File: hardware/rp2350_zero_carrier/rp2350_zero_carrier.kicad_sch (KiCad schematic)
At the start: 10 parts, among them J1 RP2350-Zero_Header(23pin,GPIO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, J2 USB-A_Host(Neltron_5075AR-04-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, J3 RP2350-Zero_Header(23pin,ボード2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, SW1 1回路2接点スイッチ(3pin,NKK_115643,ON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, SW2 1回路2接点スイッチ(3pin,NKK_115643,ON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, SW3 1回路2接点スイッチ(3pin,NKK_115643,ON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, SW4 1回路2接点スイッチ(3pin,NKK_115643,ON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

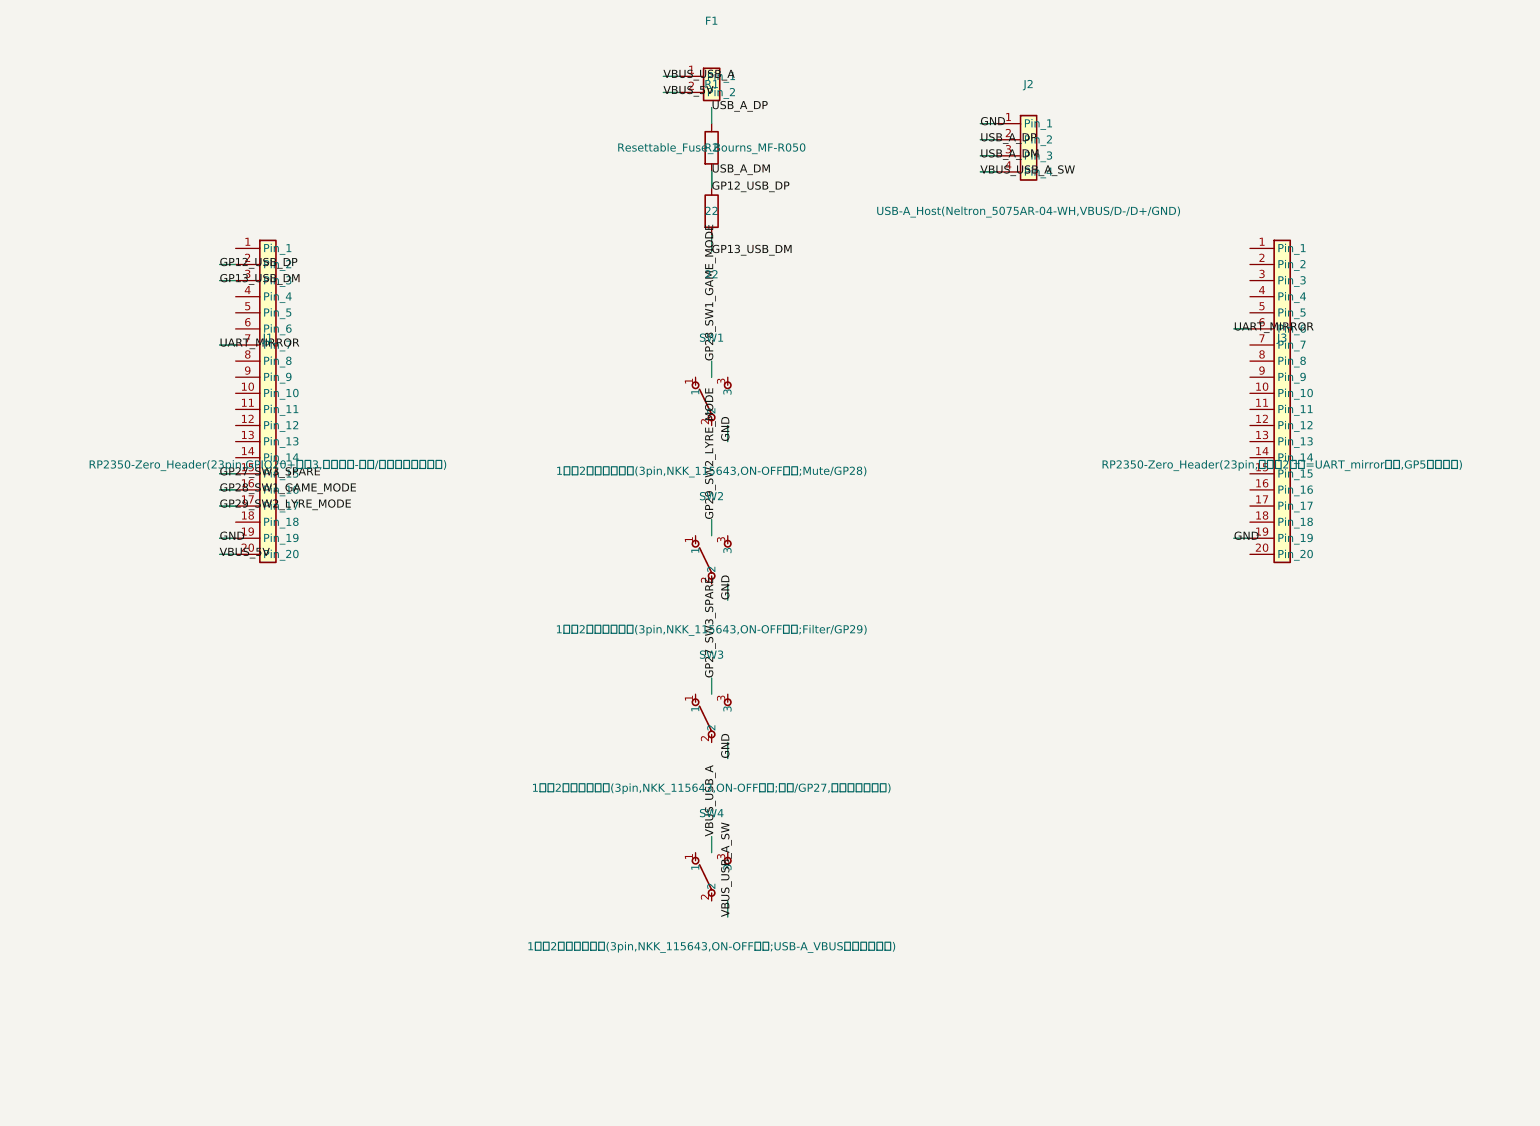
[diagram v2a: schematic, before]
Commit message: SW5(サステインスイッチ)・SW6(MIDI RESETタクトスイッチ)を回路図に追加、UART0デバッグ用ネットも定義
- SW5: SW1-4と同一のSW_SPDT_NKK_115643_Slideを再利用。中央コモンをJ3のGP29
  (net GP29_SW5_SUSTAIN)へ、片側接点をGNDへ、残り1接点はNC(issue #8のサステイン
  スイッチ、ファームはPR #9で対応済み)。
- SW6: 汎用Connector_Generic:Conn_01x04を4pinタクトスイッチの回路図表現として
  流用(内部結線が未確定なため、pin1/2をGND、pin3/4をJ3のGP28(net
  GP28_SW6_RESET)へそれぞれ束ねる防御的配線。issue #6のMIDI RESETボタン、
  ファームはPR #9で対応済み)。
- UART0デバッグ(GP0=TX/GP1=RX)をJ1・J3それぞれの回路図ピンからラベル引き出しの
  みで露出(GP0_UART0_TX/GP1_UART0_RX = J1側、J3_GP0_UART0_TX/J3_GP1_UART0_RX =
  J3側)。ユーザー指示によりピンヘッダ部品は置かず、基板側のみでテストポイントの
  スルーホールを用意する(pcb側の対応footprintは別コミット)。

kicad-cli sch erc で確認: 新規追加分はすべて既存パターンと同種の警告
(endpoint_off_grid / isolated_pin_label 等、手書きスキーマ全体に元々ある
傾向)にとどまり、新しい種類の問題は無い。pin_not_connectedはむしろ
42→39件に減少(J1/J3のGP0/GP1ピンが新規接続されたため)。

Co-Authored-By: Claude Sonnet 5 <noreply@anthropic.com>
Claude-Session: https://claude.ai/code/session_01AwWZfQU4trNEZXtx5MYHvu
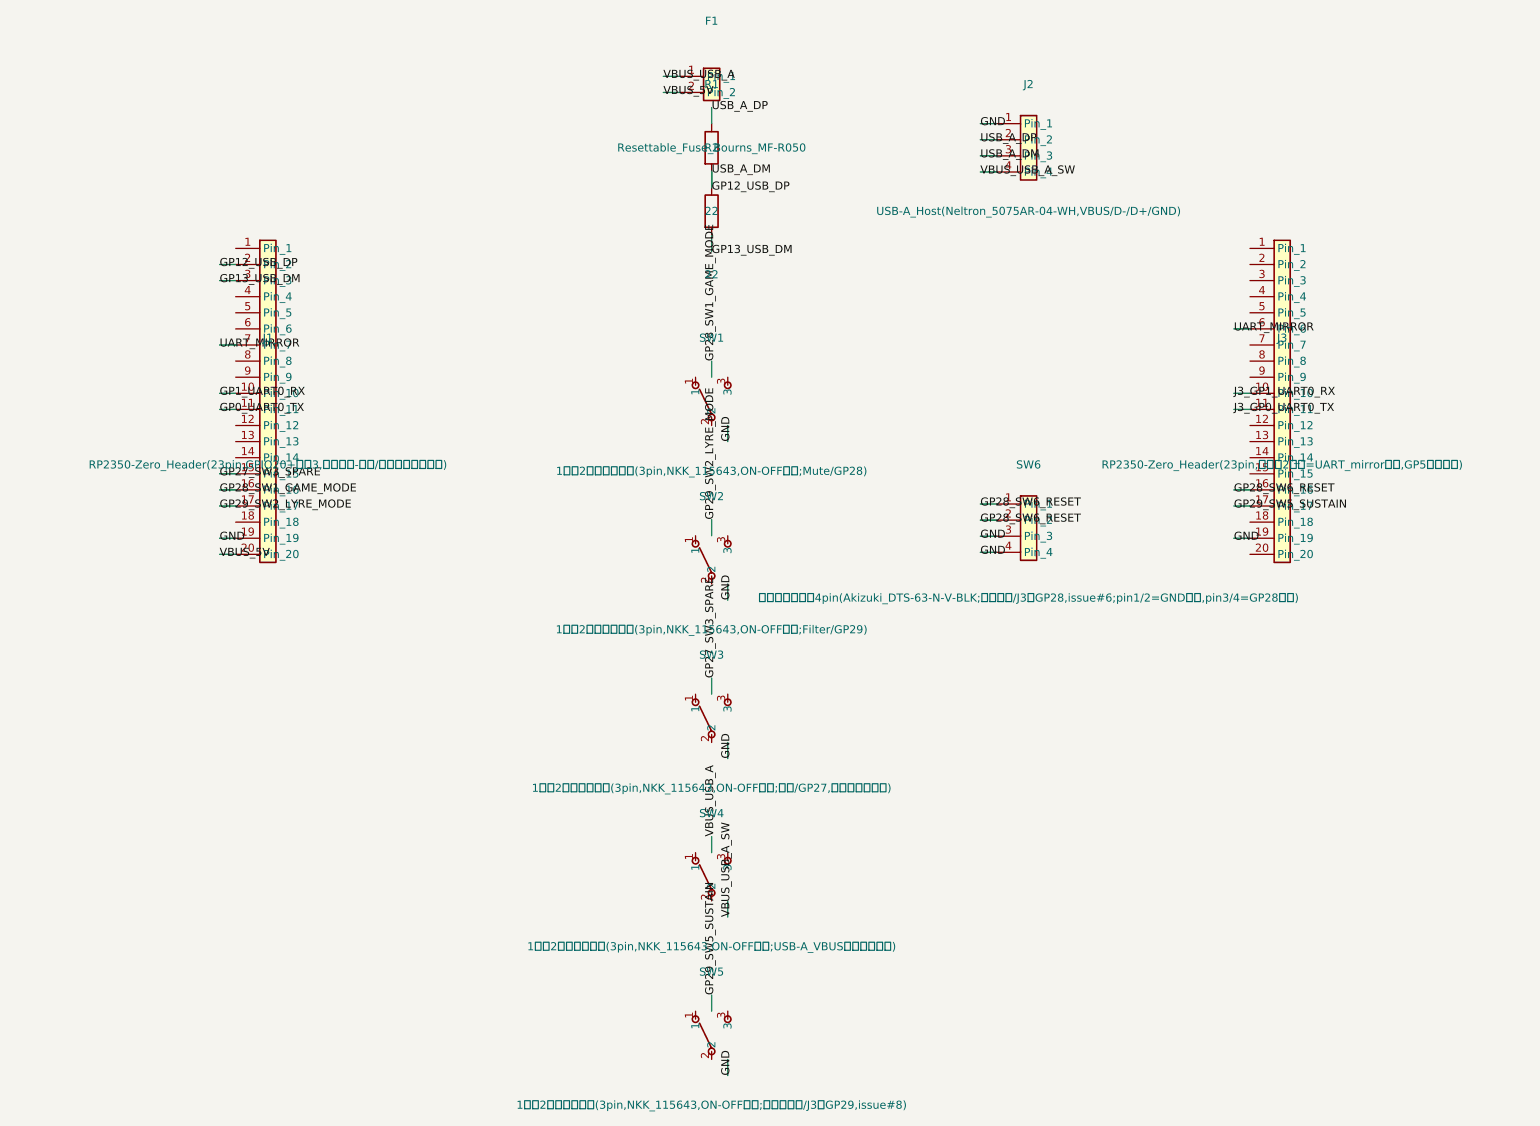
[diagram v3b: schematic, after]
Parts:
- added SW5: 1回路2接点スイッチ(3pin,NKK_115643,ON-OFF用途;サステイン/J3のGP29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, rp2350_zero_carrier:SW_SPDT_NKK_115643_Slide, symbol Switch:SW_SPDT
- added SW6: タクトスイッチ4pin(Akizuki_DTS-63-N-V-BLK;リセット/J3のGP28,i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, rp2350_zero_carrier:SW_TACT_Akizuki_DTS63, symbol Connector_Generic:Conn_01x04
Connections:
- net GND: now also SW6.3 (Pin_3), SW6.4 (Pin_4)
- net GP1_UART0_RX: now reaches J1.10 (Pin_10)
- net GP0_UART0_TX: now reaches J1.11 (Pin_11)
- net J3_GP1_UART0_RX: now reaches J3.10 (Pin_10)
- net J3_GP0_UART0_TX: now reaches J3.11 (Pin_11)
- net GP28_SW6_RESET: now reaches J3.16 (Pin_16)
- net GP28_SW6_RESET: now also SW6.1 (Pin_1), SW6.2 (Pin_2)
- net GP29_SW5_SUSTAIN: now reaches J3.17 (Pin_17)
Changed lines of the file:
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@@
+    )
+  )
+  (symbol (lib_id "Switch:SW_SPDT") (at 110 230 0) (unit 1)
+    (in_bom yes) (on_board yes) (dnp no) (fields_autoplaced yes)
+    (property "Reference" "SW5" (at 110 220 0) (effects (font (size 1.27 1.27))))
+    (property "Value" "1回路2接点スイッチ(3pin,NKK_115643,ON-OFF用途;サステイン/J3のGP29,issue#8)" (at 110 241 0) (effects (font (size 1.27 1.27))))
+    (property "Footprint" "rp2350_zero_carrier:SW_SPDT_NKK_115643_Slide" (at 110 230 0) (effects (font (size 1.27 1.27)) hide))
+    (property "Datasheet" "" (at 110 230 0) (effects (font (size 1.27 1.27)) hide))
+    (pin "1")
+    (pin "2")
+    (pin "3")
+    (instances
+      (project "rp2350_zero_carrier"
+        (path "/"
+          (reference "SW5") (unit 1)
+        )
+      )
+    )
+  )
+  (symbol (lib_id "Connector_Generic:Conn_01x04") (at 160 150 0) (unit 1)
+    (in_bom yes) (on_board yes) (dnp no) (fields_autoplaced yes)
+    (property "Reference" "SW6" (at 160 140 0) (effects (font (size 1.27 1.27))))
+    (property "Value" "タクトスイッチ4pin(Akizuki_DTS-63-N-V-BLK;リセット/J3のGP28,issue#6;pin1/2=GND束ね,pin3/4=GP28束ね)" (at 160 161 0) (effects (font (size 1.27 1.27))))
+    (property "Footprint" "rp2350_zero_carrier:SW_TACT_Akizuki_DTS63" (at 160 150 0) (effects (font (size 1.27 1.27)) hide))
+    (property "Datasheet" "" (at 160 150 0) (effects (font (size 1.27 1.27)) hide))
+    (pin "1")
+    (pin "2")
+    (pin "3")
+    (pin "4")
+    (instances
+      (project "rp2350_zero_carrier"
+        (path "/"
+          (reference "SW6") (unit 1)
+        )
+      )
     )
   )
@@
   (label "GND" (at 192.38 151.59 0) (effects (font (size 1.27 1.27)) (justify left)))
   (label "UART_MIRROR" (at 192.38 118.57 0) (effects (font (size 1.27 1.27)) (justify left)))
+  (wire (pts (xy 34.92 131.27) (xy 32.38 131.27)) (stroke (width 0) (type default)))
+  (wire (pts (xy 34.92 128.73) (xy 32.38 128.73)) (stroke (width 0) (type default)))
+  (wire (pts (xy 194.92 131.27) (xy 192.38 131.27)) (stroke (width 0) (type default)))
+  (wire (pts (xy 194.92 128.73) (xy 192.38 128.73)) (stroke (width 0) (type default)))
+  (wire (pts (xy 194.92 146.51) (xy 192.38 146.51)) (stroke (width 0) (type default)))
+  (wire (pts (xy 194.92 143.97) (xy 192.38 143.97)) (stroke (width 0) (type default)))
+  (wire (pts (xy 110 226.19) (xy 110 223.65)) (stroke (width 0) (type default)))
+  (wire (pts (xy 112.54 233.81) (xy 112.54 236.35)) (stroke (width 0) (type default)))
+  (wire (pts (xy 154.92 153.81) (xy 152.38 153.81)) (stroke (width 0) (type default)))
+  (wire (pts (xy 154.92 151.27) (xy 152.38 151.27)) (stroke (width 0) (type default)))
+  (wire (pts (xy 154.92 148.73) (xy 152.38 148.73)) (stroke (width 0) (type default)))
+  (wire (pts (xy 154.92 146.19) (xy 152.38 146.19)) (stroke (width 0) (type default)))
+  (label "GP0_UART0_TX" (at 32.38 131.27 0) (effects (font (size 1.27 1.27)) (justify left)))
+  (label "GP1_UART0_RX" (at 32.38 128.73 0) (effects (font (size 1.27 1.27)) (justify left)))
+  (label "J3_GP0_UART0_TX" (at 192.38 131.27 0) (effects (font (size 1.27 1.27)) (justify left)))
+  (label "J3_GP1_UART0_RX" (at 192.38 128.73 0) (effects (font (size 1.27 1.27)) (justify left)))
+  (label "GP29_SW5_SUSTAIN" (at 192.38 146.51 0) (effects (font (size 1.27 1.27)) (justify left)))
+  (label "GP28_SW6_RESET" (at 192.38 143.97 0) (effects (font (size 1.27 1.27)) (justify left)))
+  (label "GP29_SW5_SUSTAIN" (at 110 223.65 90) (effects (font (size 1.27 1.27)) (justify left)))
+  (label "GND" (at 112.54 236.35 90) (effects (font (size 1.27 1.27)) (justify left)))
+  (label "GND" (at 152.38 153.81 0) (effects (font (size 1.27 1.27)) (justify left)))
+  (label "GND" (at 152.38 151.27 0) (effects (font (size 1.27 1.27)) (justify left)))
+  (label "GP28_SW6_RESET" (at 152.38 148.73 0) (effects (font (size 1.27 1.27)) (justify left)))
+  (label "GP28_SW6_RESET" (at 152.38 146.19 0) (effects (font (size 1.27 1.27)) (justify left)))
   (sheet_instances
     (path "/" (page "1"))

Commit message: 回路図: UART1逆方向(J3 GP4→J1 GP5)をUART_MIRROR_RETURNとして追加
現状J1 GP4(UART1 TX)→J3 GP5(UART1 RX)のみ結線(ネットUART_MIRROR)。
UART1を双方向化するため、逆方向のJ1 GP5(UART1 RX)←J3 GP4(UART1 TX)を
新規ネットUART_MIRROR_RETURNとして追加した。GP4/GP5とも両基板側で元々
UART1のTX/RXペアとして存在する既存ピンのため新規シンボルは不要、
既存のConn_01x20(J1/J3)シンボルの未使用ピンにラベルを追加しただけ。

ラベル位置は既存のGP0/GP1(UART0デバッグ)・UART_MIRROR(GP4/GP5)ラベルと
同じ2.54mmピッチの並びに合わせて配置(J1側はGP4ラベルの1つ下、J3側は
GP5ラベルの1つ上)。kicad-cli sch ercで、この変更により新たに発生した
実質的な違反が無いことを確認済み(pin_not_connectedが2件解消され、
同数のendpoint_off_grid警告に置き換わったのみ。このendpoint_off_grid警告
自体はこのファイル内のほぼ全てのシンボル-ラベル間ワイヤーに元々存在する
既知の無害なコズメティック警告であり、今回の変更固有の問題ではない)。

ファームウェア対応は別タスク(GP4/GP5とも既存ピンの逆方向結線のみで、
新規ハードウェアの追加は無い)。

Co-Authored-By: Claude Sonnet 5 <noreply@anthropic.com>
Claude-Session: https://claude.ai/code/session_01AwWZfQU4trNEZXtx5MYHvu
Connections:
- net UART_MIRROR_RETURN: now reaches J1.6 (Pin_6)
- net UART_MIRROR_RETURN: now also J3.7 (Pin_7)
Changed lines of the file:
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@@
   (wire (pts (xy 194.92 151.59) (xy 192.38 151.59)) (stroke (width 0) (type default)))
   (wire (pts (xy 194.92 118.57) (xy 192.38 118.57)) (stroke (width 0) (type default)))
+  (wire (pts (xy 34.92 118.57) (xy 32.38 118.57)) (stroke (width 0) (type default)))
+  (wire (pts (xy 194.92 121.11) (xy 192.38 121.11)) (stroke (width 0) (type default)))
   (wire (pts (xy 110 93.81) (xy 110 96.35)) (stroke (width 0) (type default)))
   (wire (pts (xy 110 86.19) (xy 110 83.65)) (stroke (width 0) (type default)))
@@
   (label "GND" (at 192.38 151.59 0) (effects (font (size 1.27 1.27)) (justify left)))
   (label "UART_MIRROR" (at 192.38 118.57 0) (effects (font (size 1.27 1.27)) (justify left)))
+  (label "UART_MIRROR_RETURN" (at 32.38 118.57 0) (effects (font (size 1.27 1.27)) (justify left)))
+  (label "UART_MIRROR_RETURN" (at 192.38 121.11 0) (effects (font (size 1.27 1.27)) (justify left)))
   (wire (pts (xy 34.92 131.27) (xy 32.38 131.27)) (stroke (width 0) (type default)))
   (wire (pts (xy 34.92 128.73) (xy 32.38 128.73)) (stroke (width 0) (type default)))
